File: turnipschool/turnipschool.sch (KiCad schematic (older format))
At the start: 60 parts, among them J1 USB-DEVICE-SHIELD, P1 CONN_1, P2 RESET_N, P3 DD, P4 DC, P5 3V3, P6 GND, P7 CABLE, T1 BALUN, U1 CC1111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

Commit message: changed R17 part selection to 0402
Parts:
- R17: Description RES 1.50K OHM 1/10W 1% 0603 SMD -> RES SMD 1.5K OHM 1% 1/16W 0402; Part Number MCR03ERTF1501 -> MCR01MRTF1501
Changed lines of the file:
@@
 F 3 "" H 7950 5250 60  0001 C CNN
 F 4 "Rohm" H 7950 5250 60  0001 C CNN "Manufacturer"
-F 5 "MCR03ERTF1501" H 7950 5250 60  0001 C CNN "Part Number"
-F 6 "RES 1.50K OHM 1/10W 1% 0603 SMD" H 7950 5250 60  0001 C CNN "Description"
+F 5 "MCR01MRTF1501" H 7950 5250 60  0001 C CNN "Part Number"
+F 6 "RES SMD 1.5K OHM 1% 1/16W 0402" H 7950 5250 60  0001 C CNN "Description"
 F 7 "1%" V 7850 5250 60  0000 C CNN "Note"
 	1    7950 5250

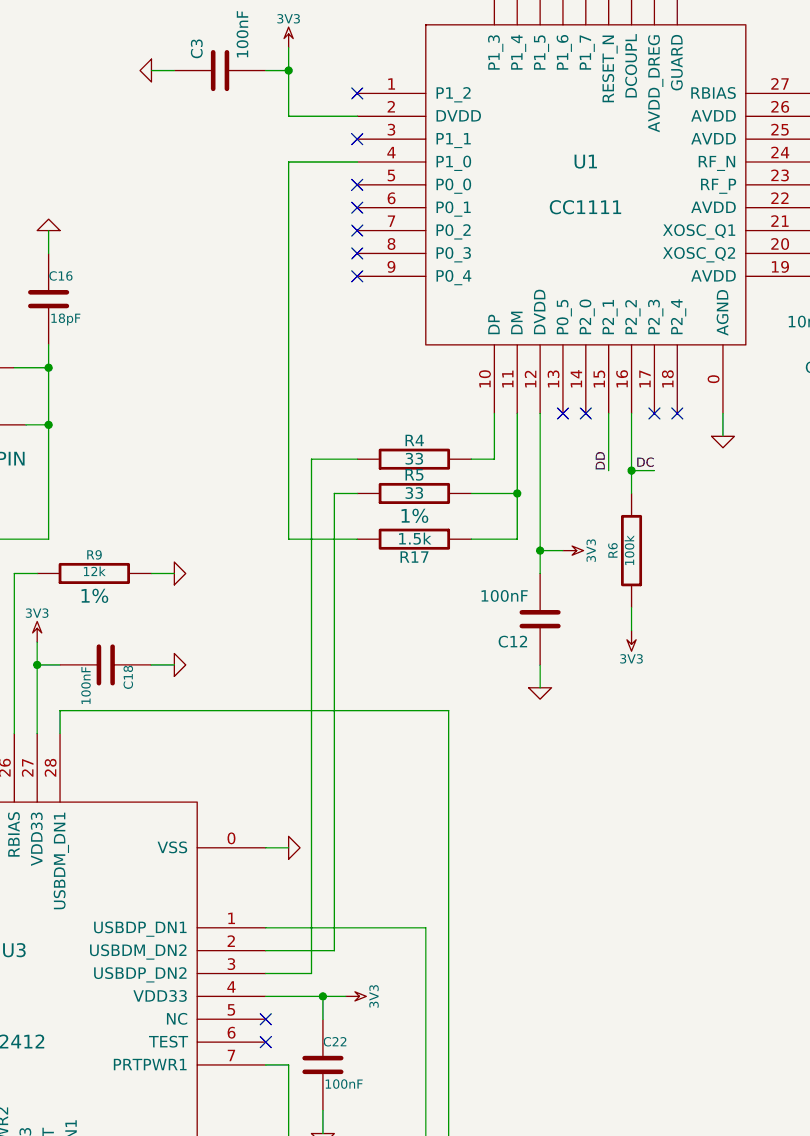
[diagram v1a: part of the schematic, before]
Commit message: moved R17 from DM to DP
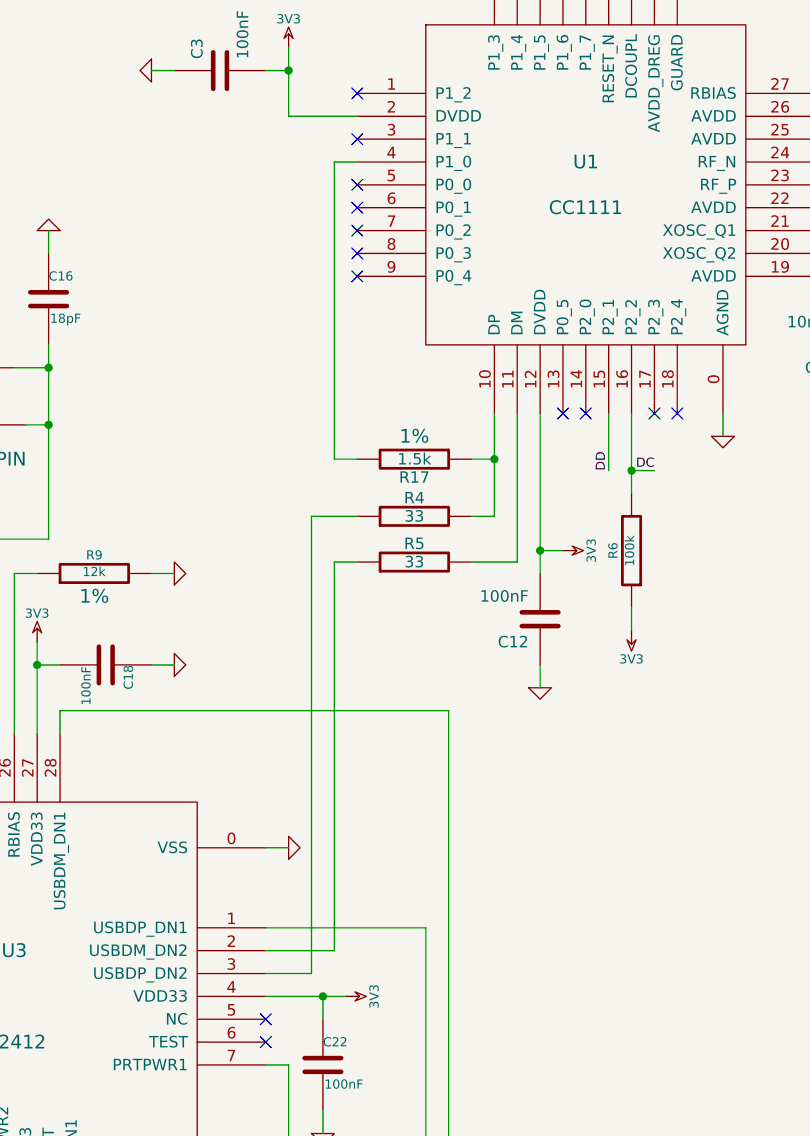
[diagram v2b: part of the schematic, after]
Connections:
- net at R4.2, U1.10 (DP): now also R17.1
- net at R5.2, U1.11 (DM): no longer R17.1
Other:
- moved on the sheet: R17, R4, R5
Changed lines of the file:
@@
 L R R5
 U 1 1 504CAEA4
-P 7950 5050
-F 0 "R5" V 8030 5050 50  0000 C CNN
-F 1 "33" V 7950 5050 50  0000 C CNN
-F 2 "cc1111-legacy:GSG-0402" H 7950 5050 60  0001 C CNN
-F 3 "" H 7950 5050 60  0001 C CNN
-F 4 "Samsung Electro-Mechanics America, Inc" H 7950 5050 60  0001 C CNN "Manufacturer"
-F 5 "RC1005J330CS" H 7950 5050 60  0001 C CNN "Part Number"
-F 6 "RES 33 OHM 1/16W 5% 0402" H 7950 5050 60  0001 C CNN "Description"
-	1    7950 5050
+P 7950 5350
+F 0 "R5" V 8030 5350 50  0000 C CNN
+F 1 "33" V 7950 5350 50  0000 C CNN
+F 2 "cc1111-legacy:GSG-0402" H 7950 5350 60  0001 C CNN
+F 3 "" H 7950 5350 60  0001 C CNN
+F 4 "Samsung Electro-Mechanics America, Inc" H 7950 5350 60  0001 C CNN "Manufacturer"
+F 5 "RC1005J330CS" H 7950 5350 60  0001 C CNN "Part Number"
+F 6 "RES 33 OHM 1/16W 5% 0402" H 7950 5350 60  0001 C CNN "Description"
+	1    7950 5350
 	0    -1   -1   0
 $EndComp
@@
 L R R4
 U 1 1 504CAE9B
-P 7950 4900
-F 0 "R4" V 8030 4900 50  0000 C CNN
-F 1 "33" V 7950 4900 50  0000 C CNN
-F 2 "cc1111-legacy:GSG-0402" H 7950 4900 60  0001 C CNN
-F 3 "" H 7950 4900 60  0001 C CNN
-F 4 "Samsung Electro-Mechanics America, Inc" H 7950 4900 60  0001 C CNN "Manufacturer"
-F 5 "RC1005J330CS" H 7950 4900 60  0001 C CNN "Part Number"
-F 6 "RES 33 OHM 1/16W 5% 0402" H 7950 4900 60  0001 C CNN "Description"
-	1    7950 4900
+P 7950 5150
+F 0 "R4" V 8030 5150 50  0000 C CNN
+F 1 "33" V 7950 5150 50  0000 C CNN
+F 2 "cc1111-legacy:GSG-0402" H 7950 5150 60  0001 C CNN
+F 3 "" H 7950 5150 60  0001 C CNN
+F 4 "Samsung Electro-Mechanics America, Inc" H 7950 5150 60  0001 C CNN "Manufacturer"
+F 5 "RC1005J330CS" H 7950 5150 60  0001 C CNN "Part Number"
+F 6 "RES 33 OHM 1/16W 5% 0402" H 7950 5150 60  0001 C CNN "Description"
+	1    7950 5150
 	0    -1   -1   0
 $EndComp
@@
 Wire Wire Line
 	6300 5800 6400 5800
-Wire Wire Line
-	7700 4900 7500 4900
-Wire Wire Line
-	8300 4900 8200 4900
-Wire Wire Line
-	8300 4700 8300 4900
-Wire Wire Line
-	7700 5050 7600 5050
 Connection ~ 8900 4950
 Wire Wire Line
@@
 Wire Wire Line
 	8800 2400 8800 2700
-Wire Wire Line
-	8400 4700 8400 5250
-Wire Wire Line
-	8400 5050 8200 5050
 Wire Wire Line
 	9700 9950 9700 9850
@@
 L R R17
 U 1 1 549012D7
-P 7950 5250
-F 0 "R17" V 8030 5250 50  0000 C CNN
-F 1 "1.5k" V 7950 5250 50  0000 C CNN
-F 2 "cc1111-legacy:GSG-0402" H 7950 5250 60  0001 C CNN
-F 3 "" H 7950 5250 60  0001 C CNN
-F 4 "Rohm" H 7950 5250 60  0001 C CNN "Manufacturer"
-F 5 "MCR01MRTF1501" H 7950 5250 60  0001 C CNN "Part Number"
-F 6 "RES SMD 1.5K OHM 1% 1/16W 0402" H 7950 5250 60  0001 C CNN "Description"
-F 7 "1%" V 7850 5250 60  0000 C CNN "Note"
-	1    7950 5250
+P 7950 4900
+F 0 "R17" V 8030 4900 50  0000 C CNN
+F 1 "1.5k" V 7950 4900 50  0000 C CNN
+F 2 "cc1111-legacy:GSG-0402" H 7950 4900 60  0001 C CNN
+F 3 "" H 7950 4900 60  0001 C CNN
+F 4 "Rohm" H 7950 4900 60  0001 C CNN "Manufacturer"
+F 5 "MCR01MRTF1501" H 7950 4900 60  0001 C CNN "Part Number"
+F 6 "RES SMD 1.5K OHM 1% 1/16W 0402" H 7950 4900 60  0001 C CNN "Description"
+F 7 "1%" V 7850 4900 60  0000 C CNN "Note"
+	1    7950 4900
 	0    1    1    0
 $EndComp
@@
 Wire Wire Line
 	7300 7150 7500 7150
-Wire Wire Line
-	7500 7150 7500 4900
 Wire Wire Line
 	8100 8350 8100 6000
@@
 Wire Wire Line
 	8500 5300 8600 5300
-Wire Wire Line
-	8400 5250 8200 5250
-Connection ~ 8400 5050
-Wire Wire Line
-	7600 5050 7600 7050
-Wire Wire Line
-	7700 5250 7400 5250
-Wire Wire Line
-	7400 5250 7400 3600
-Wire Wire Line
-	7400 3600 7700 3600
 $Comp
 L R R6
@@
 	-1   0    0    1
 $EndComp
+Wire Wire Line
+	8300 4700 8300 5150
+Wire Wire Line
+	8300 4900 8200 4900
+Wire Wire Line
+	8300 5150 8200 5150
+Connection ~ 8300 4900
+Wire Wire Line
+	7500 7150 7500 5150
+Wire Wire Line
+	7500 5150 7700 5150
+Wire Wire Line
+	7600 7050 7600 5350
+Wire Wire Line
+	7600 5350 7700 5350
+Wire Wire Line
+	7700 3600 7600 3600
+Wire Wire Line
+	7600 3600 7600 4900
+Wire Wire Line
+	7600 4900 7700 4900
+Wire Wire Line
+	8200 5350 8400 5350
+Wire Wire Line
+	8400 5350 8400 4700
 $EndSCHEMATC

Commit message: restored debug LED
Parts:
- added D1: LED1, symbol LED
- added R3: 330, cc1111-legacy:GSG-0402, symbol R
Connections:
- net GND: now also D1.2 (K)
- net at U1.3 (P1_1): now also R3.1
- new net: D1.1 (A), R3.2
- no-connect marks 23 -> 22
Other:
- note added: "Populate only for test and debug."

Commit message: remembered to save schematic
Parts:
- D1: footprint (none) -> cc1111-legacy:GSG-0603D
